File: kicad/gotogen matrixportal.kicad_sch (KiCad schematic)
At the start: 27 parts, among them J1 HUB75 Out, J2 HUB75 In, J3 OLED_128_64, J4 Buttons EXT, J5 OpenMV, J6 Extra Connections, J7 Capacitive Touch, SW1 Back, SW2 Menu, SW3 Up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

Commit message: first pass at pcb update
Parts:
- added SW7: Reset, Button_Switch_THT:SW_PUSH_6mm, symbol Switch:SW_Push
- J6: footprint Connector_PinHeader_2.54mm:PinHeader_1x06_P2.54mm_Vertical -> Connector_PinHeader_2.54mm:PinHeader_1x05_P2.54mm_Vertical; symbol Connector_Generic:Conn_01x06 -> Connector_Generic:Conn_01x05
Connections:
- net A_GND is gone; now on net GND: JP2.1 (A), JP3.1 (A), U5.1 (GND)
- net A_VDD is gone; now on net +3.3V: JP2.3 (B), JP3.3 (B), U5.2 (Vdd)
- net GND: now also J6.5 (Pin_5), U2.2 (GND), SW7.1; no longer J6.6 (Pin_6)
- net PB07: now also J6.4 (Pin_4); no longer J6.5 (Pin_5)
- net PB13: now also J6.2 (Pin_2); no longer J6.3 (Pin_3)
- net PB14: now also J6.3 (Pin_3); no longer J6.4 (Pin_4)
- net at U1.1 (RST): now also SW7.2
- net MIC: now reaches U5.4 (Out)
- net MIC: now also U1.9 (A4/PA07)
- net A_GAIN renamed GAIN
- removed net PA07: J6.2 (Pin_2), U1.9 (A4/PA07)
- no-connect marks 22 -> 19
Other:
- note added: "Unused connections from the MatrixPortal. Outputs only. 5V levels. PB13 requires bridging the E jumper on the MatrixPortal to either position."
- note removed: "U5 is connected to the MatrixPortal via the analog JST connector, which provides power and output signals. The gain can be adjusted by what that pin is connected to."
- note removed: "Unused connections from the MatrixPortal. Only PA07 can be used for input. PA07 outputs 3V3. The others ouput 5V. PB13 requires bridging the E jumper on the MatrixPortal to either position."
- company: (none) -> Andy Janata
- title: (none) -> Gotogen Matrix Portal
- moved on the sheet: C1, C2, J4, J7, JP2, JP3, JP4, R1, R2, R3, SW1, SW2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

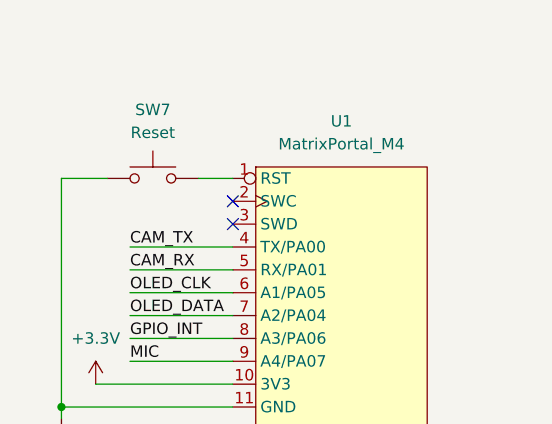
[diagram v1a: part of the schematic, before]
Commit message: completely rework PCB layout
needed to get the matrixportal further away from my face, which required
moving just about everything around
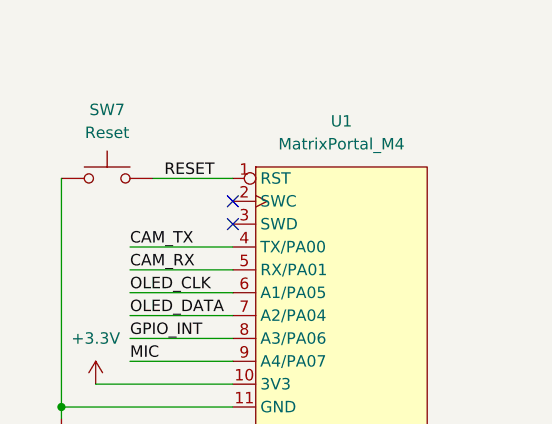
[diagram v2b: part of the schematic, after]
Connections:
- net RESET: now reaches SW7.2, U1.1 (RST)
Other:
- moved on the sheet: SW7
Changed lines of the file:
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@@
-    (stroke (width 0) (type default) (color 0 0 0 0))
-  )
-  (wire (pts (xy 27.94 33.02) (xy 22.86 33.02))
     (stroke (width 0) (type default) (color 0 0 0 0))
   )
@@
     (stroke (width 0) (type default) (color 0 0 0 0))
   )
-  (wire (pts (xy 38.1 33.02) (xy 41.91 33.02))
+  (wire (pts (xy 33.02 33.02) (xy 41.91 33.02))
     (stroke (width 0) (type default) (color 0 0 0 0))
   )
@@
   )
   (label "CT_DOWN" (at 242.57 140.97 0)
+    (effects (font (size 1.27 1.27)) (justify left bottom))
+  )
+  (label "RESET" (at 34.29 33.02 0)
     (effects (font (size 1.27 1.27)) (justify left bottom))
   )
@@
     (pin "2")
   )
-  (symbol (lib_id "Switch:SW_Push") (at 33.02 33.02 0) (unit 1)
+  (symbol (lib_id "Switch:SW_Push") (at 27.94 33.02 0) (unit 1)
     (in_bom yes) (on_board yes)
-    (property "Reference" "SW7" (id 0) (at 33.02 25.4 0))
-    (property "Value" "Reset" (id 1) (at 33.02 27.94 0))
-    (property "Footprint" "Button_Switch_THT:SW_PUSH_6mm" (id 2) (at 33.02 27.94 0)
-      (effects (font (size 1.27 1.27)) hide)
-    )
-    (property "Datasheet" "~" (id 3) (at 33.02 27.94 0)
-      (effects (font (size 1.27 1.27)) hide)
-    )
+    (property "Reference" "SW7" (id 0) (at 27.94 25.4 0))
+    (property "Value" "Reset" (id 1) (at 27.94 27.94 0))
+    (property "Footprint" "Button_Switch_THT:SW_PUSH_6mm" (id 2) (at 27.94 27.94 0)
+      (effects (font (size 1.27 1.27)) hide)
+    )
+    (property "Datasheet" "~" (id 3) (at 27.94 27.94 0)
+      (effects (font (size 1.27 1.27)) hide)
+    )
